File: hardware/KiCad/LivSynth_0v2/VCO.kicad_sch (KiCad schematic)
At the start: 26 parts, among them J15 Jumper, J16 Jumper, J17 Jumper, Q11 2N3904, Q12 2N3904, Q14 2N3904, SW1 SW_SPDT, U2 TL074, U4 TL074

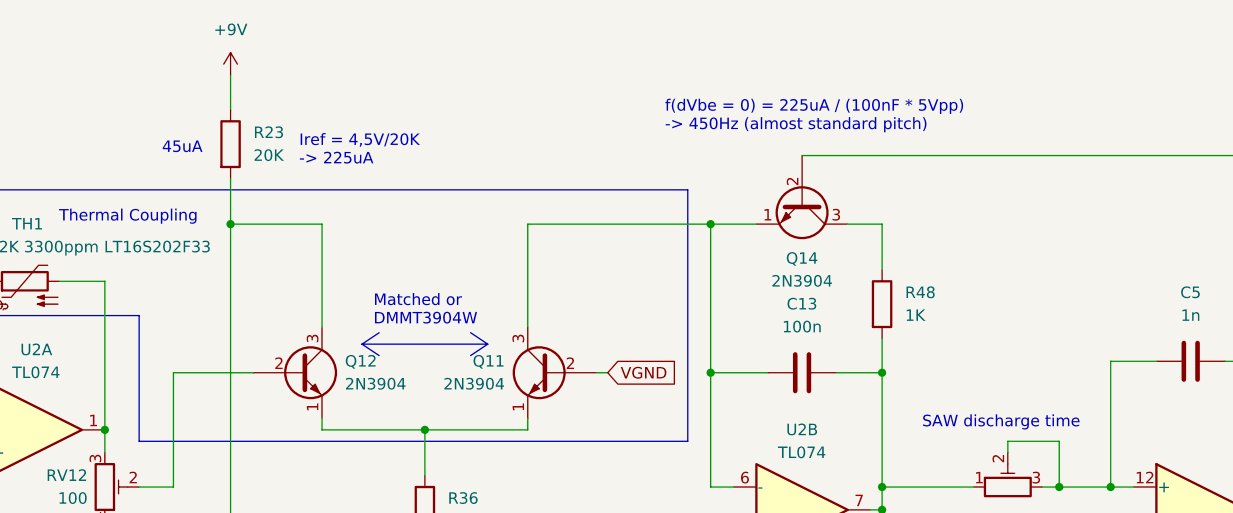
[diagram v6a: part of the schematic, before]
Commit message: Reduce EG cap to 4u7 Reduce LFO cap to 220n VCO R23: 470K, C13: 10n
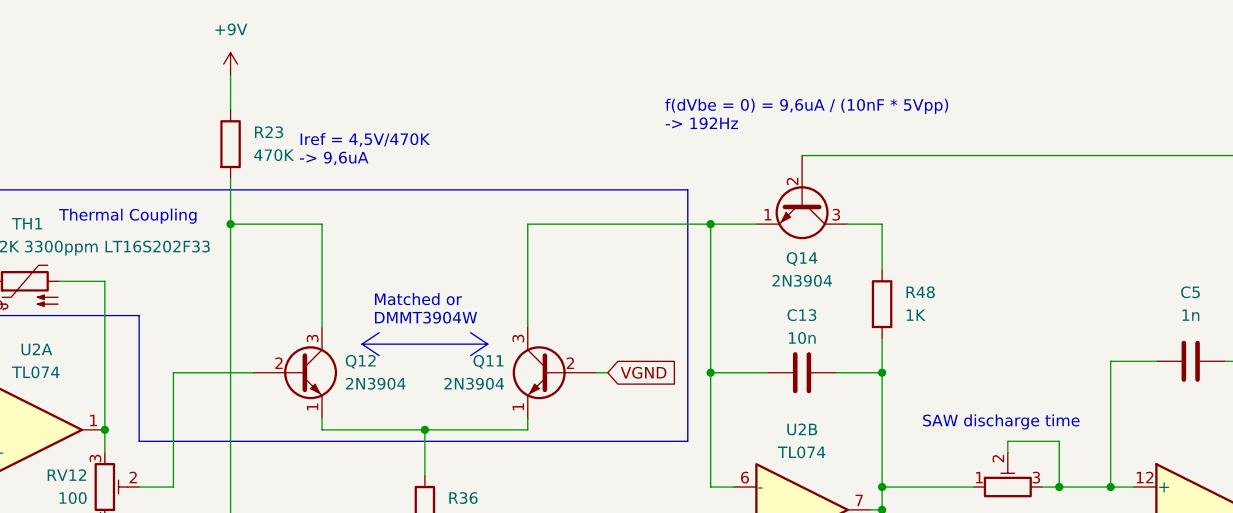
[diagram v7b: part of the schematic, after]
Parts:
- C13: value 100n -> 10n
- R23: value 20K -> 470K
- SW1: footprint SloBlo:SW_Toggle_MS500C -> SloBlo:SW_Toggle_MS500
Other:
- note added: "Iref = 4,5V/470K -> 9,6uA"
- note added: "f(dVbe = 0) = 9,6uA / (10nF * 5Vpp) -> 192Hz"
- note removed: "45uA"
- note removed: "Iref = 4,5V/20K -> 225uA"
- note removed: "f(dVbe = 0) = 225uA / (100nF * 5Vpp) -> 450Hz (almost standard pitch)"
